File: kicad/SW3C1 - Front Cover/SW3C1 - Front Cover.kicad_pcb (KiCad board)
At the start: 2 copper layers, 203.2 x 67.1 mm, 0 parts

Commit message: cleanup silkscreen
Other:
- board size 203.2 x 67.1 mm -> 203.2 x 68.6 mm
- board text added: "ADJUST"
- board text added: "CHANNEL 1"
- board text added: "CHANNEL 2"
- board text added: "CHANNEL 3"
- board text added: "CHANNEL 4"
- board text added: "DC IN"
- board text added: "EXPANSION"
- board text added: "OFF"
- board text added: "ON"
- board text added: "OUTPUTS"
- board text added: "STATUS"
- board text added: "SW32"
- board text added: "SW3C1 Rev 1"
- board text added: "TRIGGERS"
- board text removed: "Channel 1"
- board text removed: "Channel 2"
- board text removed: "Channel 3"
- board text removed: "Channel 4"
- board text removed: "DC In"
- board text removed: "Multi Adjust"

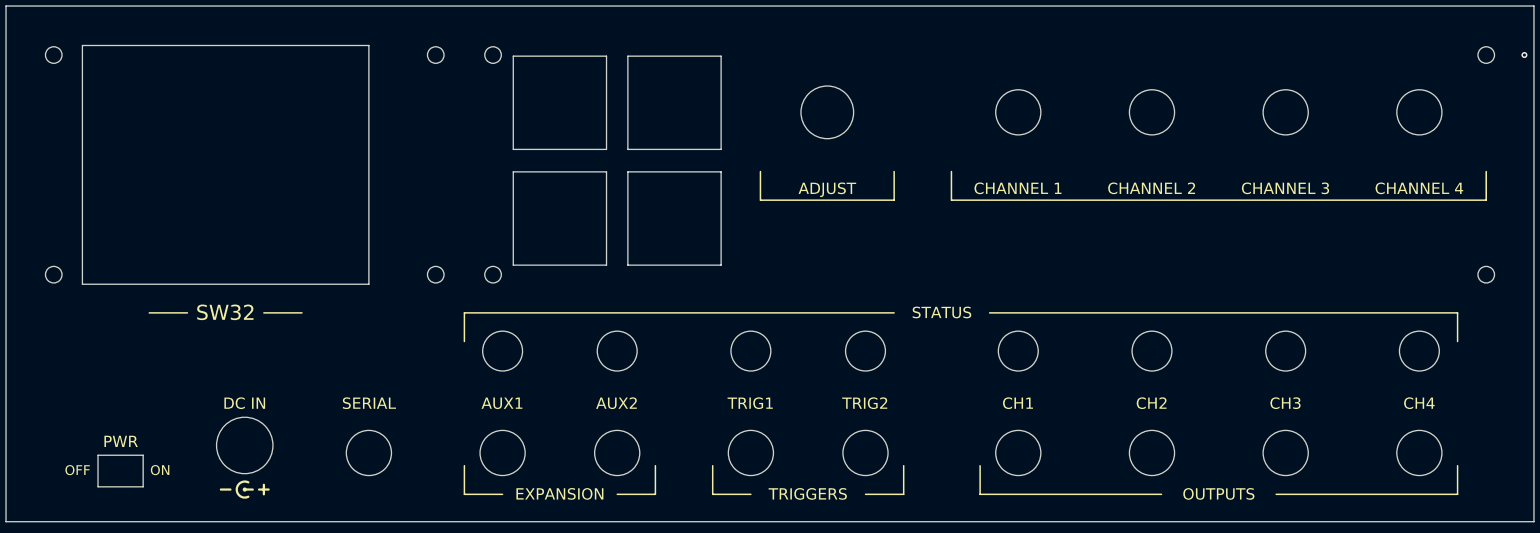
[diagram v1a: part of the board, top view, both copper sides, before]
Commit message: update tolerances
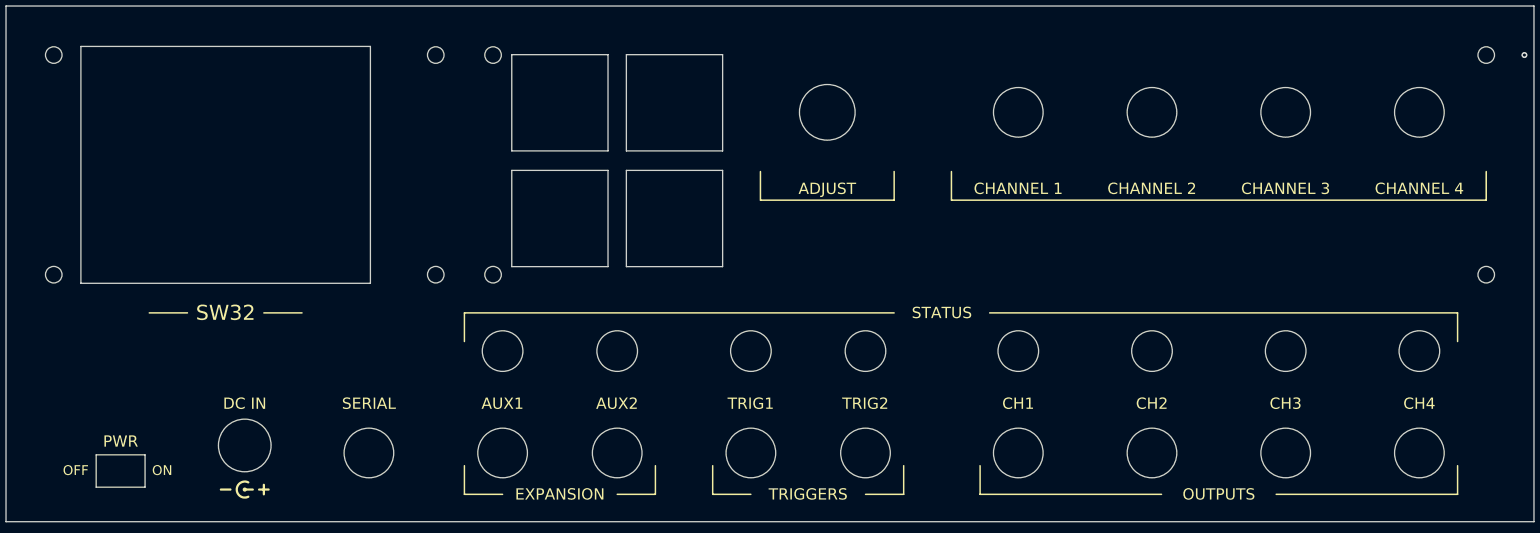
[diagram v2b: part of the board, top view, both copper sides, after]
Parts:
- added REF**: MountingHole_2.2mm_M2, MountingHole:MountingHole_2.2mm_M2, F.Cu at (116.8, 69.8)
- added REF**: MountingHole_2.2mm_M2, MountingHole:MountingHole_2.2mm_M2, F.Cu at (248.9, 69.8)
- added REF**: MountingHole_2.2mm_M2, MountingHole:MountingHole_2.2mm_M2, F.Cu at (58.4, 69.8)
- added REF**: MountingHole_2.2mm_M2, MountingHole:MountingHole_2.2mm_M2, F.Cu at (116.8, 99.1)
- added REF**: MountingHole_2.2mm_M2, MountingHole:MountingHole_2.2mm_M2, F.Cu at (248.9, 99.1)
- added REF**: MountingHole_2.2mm_M2, MountingHole:MountingHole_2.2mm_M2, F.Cu at (109.2, 99.1)
- added REF**: MountingHole_2.2mm_M2, MountingHole:MountingHole_2.2mm_M2, F.Cu at (109.2, 69.8)
- added REF**: MountingHole_2.2mm_M2, MountingHole:MountingHole_2.2mm_M2, F.Cu at (58.4, 99.1)
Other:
- outline, holes or cut-outs redrawn
